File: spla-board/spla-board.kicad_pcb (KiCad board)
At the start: 4 copper layers, 178 x 107 mm, 271 parts, among them J1 USB_B_Micro, J12 J_POWER, J13 J_ANALOG, J14 J_AREF, J15 J_DPULL, J2 J_JTAG, J3 J_BODGE, J4 J_POWER2, J5 J_PPURESET, J6 J_SAMPLE, J7 Barrel_Jack, J8 J_AREF_AMP, U1 LFE5U-45F-BG256, U10 SNES_PPU1, U11 SNES_PPU2, U12 VRAM, U13 VRAM, U14 TLV73311PDBV, U15 74LVC8T245, U16 74LVC8T245, U17 74LVC8T245, U2 FT2232H, U20 74LVC8T245, U22 74LVC8T245, U23 74LVC8T245, U24 74LVC8T245, U25 74LVC8T245, U26 74LVC8T245, U27 74LVC8T245, U28 74LVC8T245, U29 74LVC8T245, U3 93LC66B, U30 74LVC8T245, U31 74LVC8T245, U32 74LVC8T245, U51 ADC1173, U52 ADC1173, U53 ADC1173, U61 LMH6611, U62 LMH6611, U63 LMH6611, U7 ST1S10PHR, U74 LMH6611, U75 LMH6611, U76 TLV73333PDBV, U8 ST1S10PHR, U9 TLV73325PDBV, X1 FT5HNBPK12.0-T1

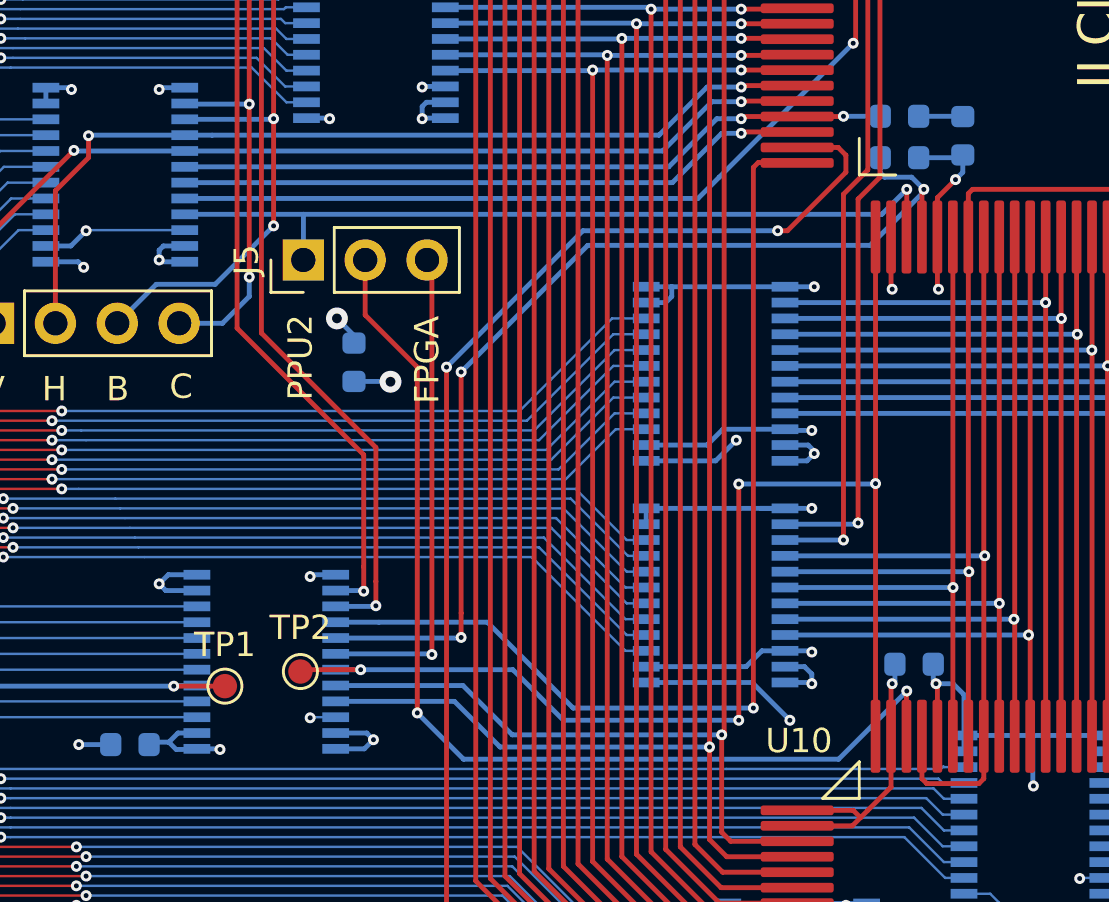
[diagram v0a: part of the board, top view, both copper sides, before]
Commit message: schematic/pcb: Move PPU RESET pulldowns before level shifter.
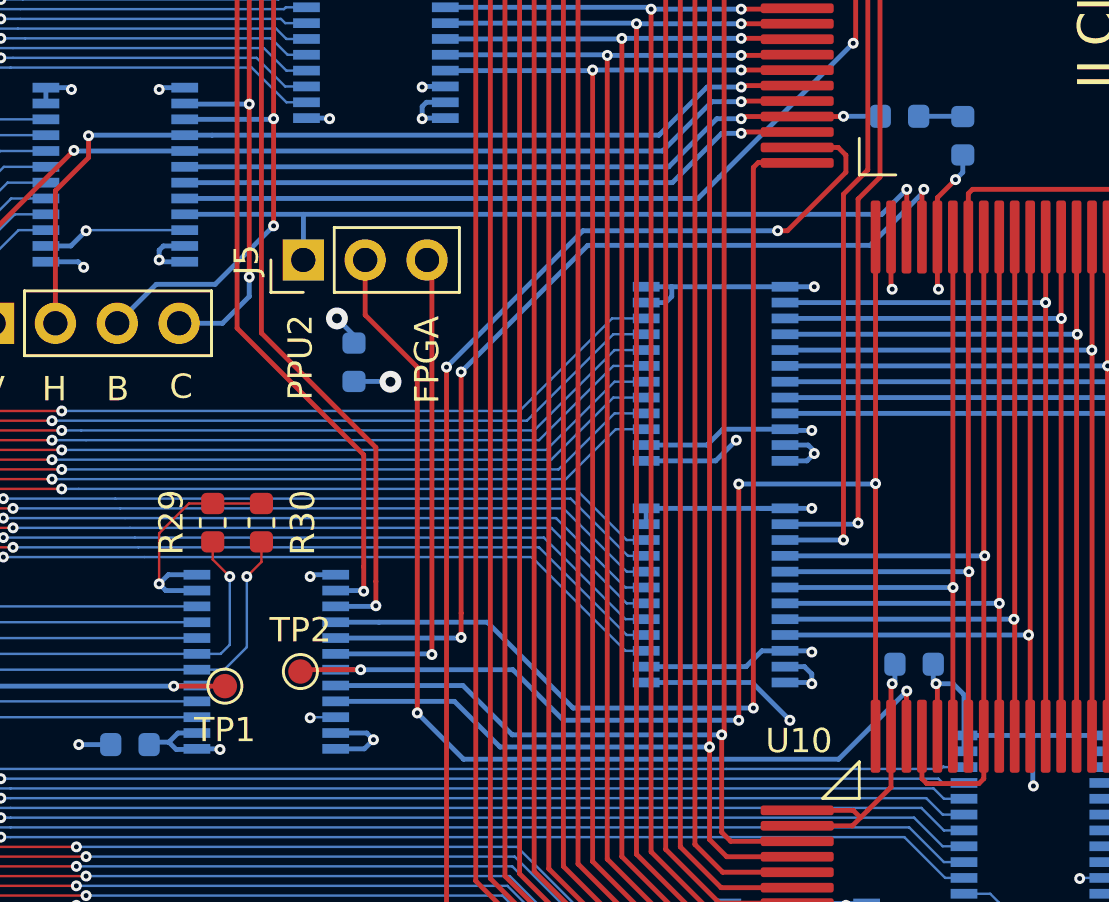
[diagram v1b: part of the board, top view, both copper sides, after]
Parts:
- added R30: 10k, Resistor_SMD:R_0603_1608Metric, F.Cu at (135.0, 100.2)
- R29: moved to F.Cu
- moved R29 31.9 mm to (133.0, 100.2), turned to 90 degrees
- renumbered R30 to R31
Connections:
- R29 pad 1: TAP_PPU2_~RESET~ -> FPGA_PPU2_~RESET~
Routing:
- net FPGA_PPU1_~RESET~: track 35.3 -> 42.3 mm, vias 1 -> 2
- net FPGA_PPU2_~RESET~: track 34.2 -> 40.2 mm, vias 1 -> 2
- net GND: track 494.1 -> 499.2 mm
- net TAP_PPU2_~RESET~: track 42.9 -> 40.2 mm

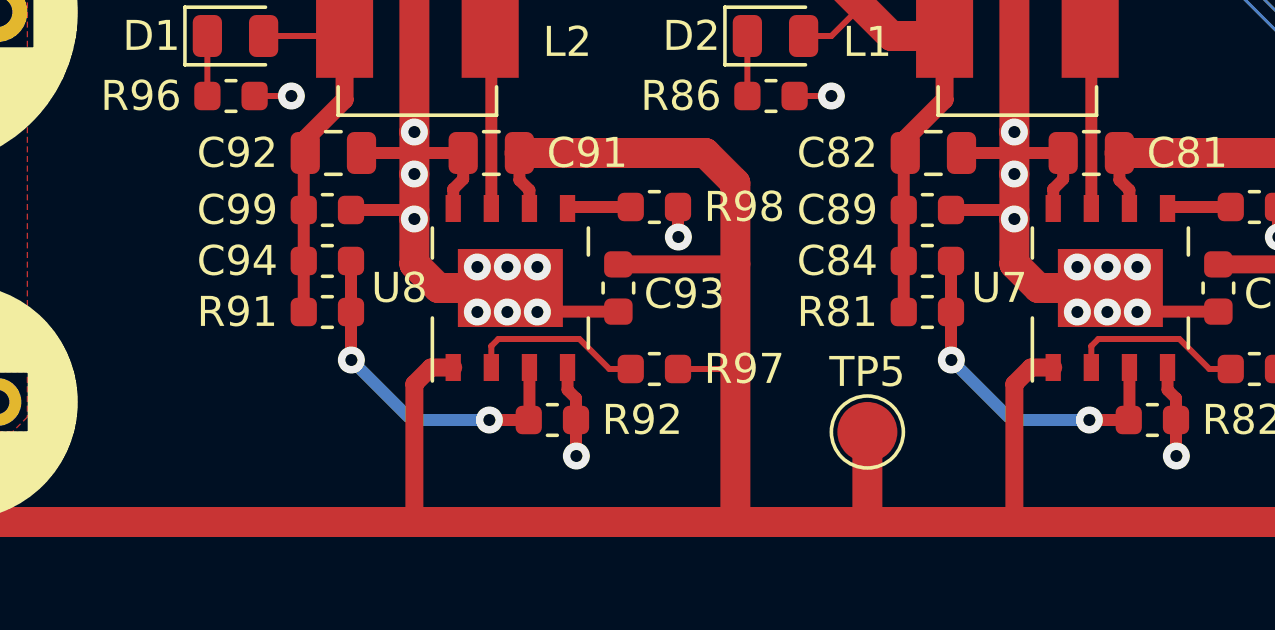
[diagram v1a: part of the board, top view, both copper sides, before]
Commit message: schematic/pcb: Complete part selection of resistors and capacitors.  Omit filters in analog block for now; adjust PCB to suit.
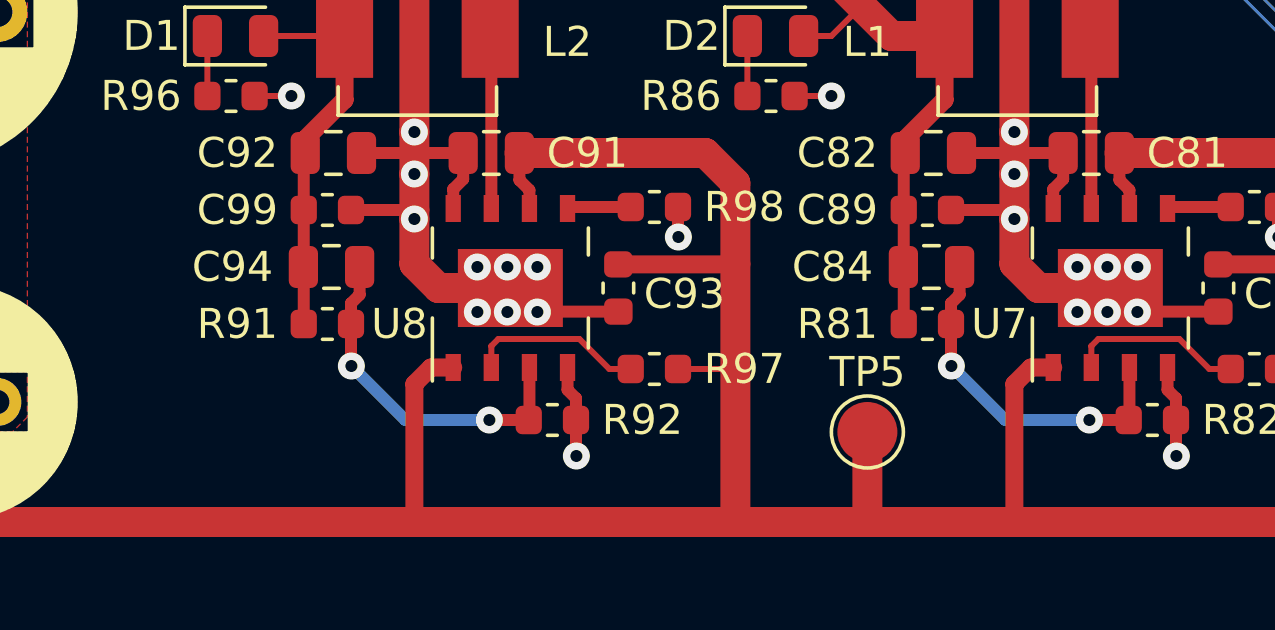
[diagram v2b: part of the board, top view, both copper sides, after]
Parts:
- C101, C102, C201, C202, C301, C302: value 1pF -> NOSTUFF
- C109, C209, C309: value 390pF -> NOSTUFF
- C7: value 3.3uF -> 4.7uF
- C84, C94: footprint Capacitor_SMD:C_0603_1608Metric -> Capacitor_SMD:C_0805_2012Metric
- R101, R102, R201, R202, R301, R302: value 16k -> 0
- R104, R204, R304: value INF -> NOSTUFF
- R109, R209, R309: value 22 -> 0
- moved R81 0.40 mm to (99.0, 144.4)
- moved R91 0.40 mm to (79.0, 144.4)
- moved C84 0.24 mm to (99.1, 142.5)
- moved C94 0.24 mm to (79.1, 142.5)

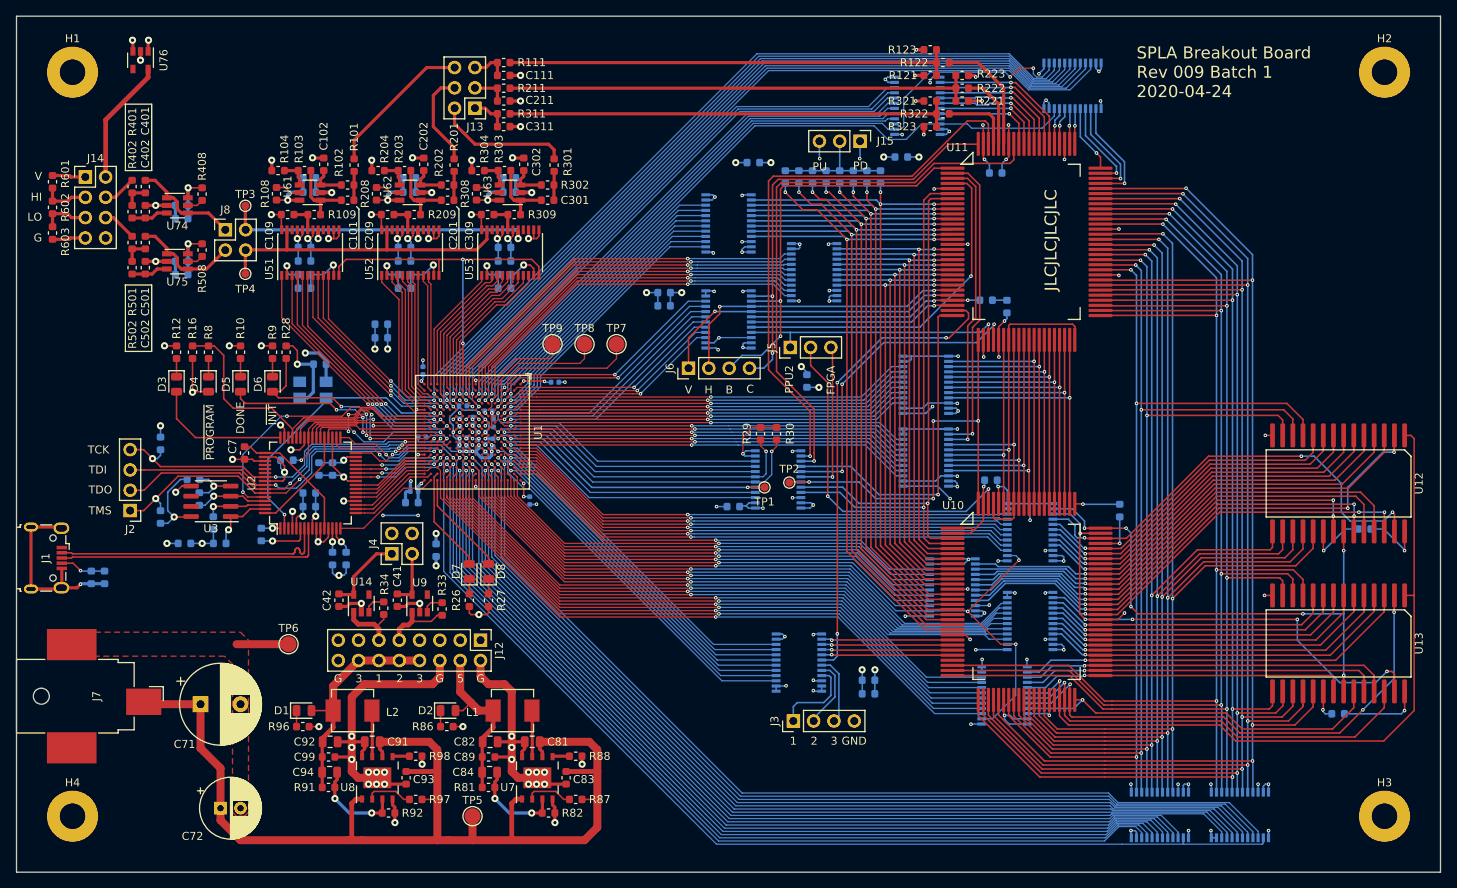
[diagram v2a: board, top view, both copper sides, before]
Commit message: pcb: Widen via-to-via distances in several places to avoid plausible drill issues.
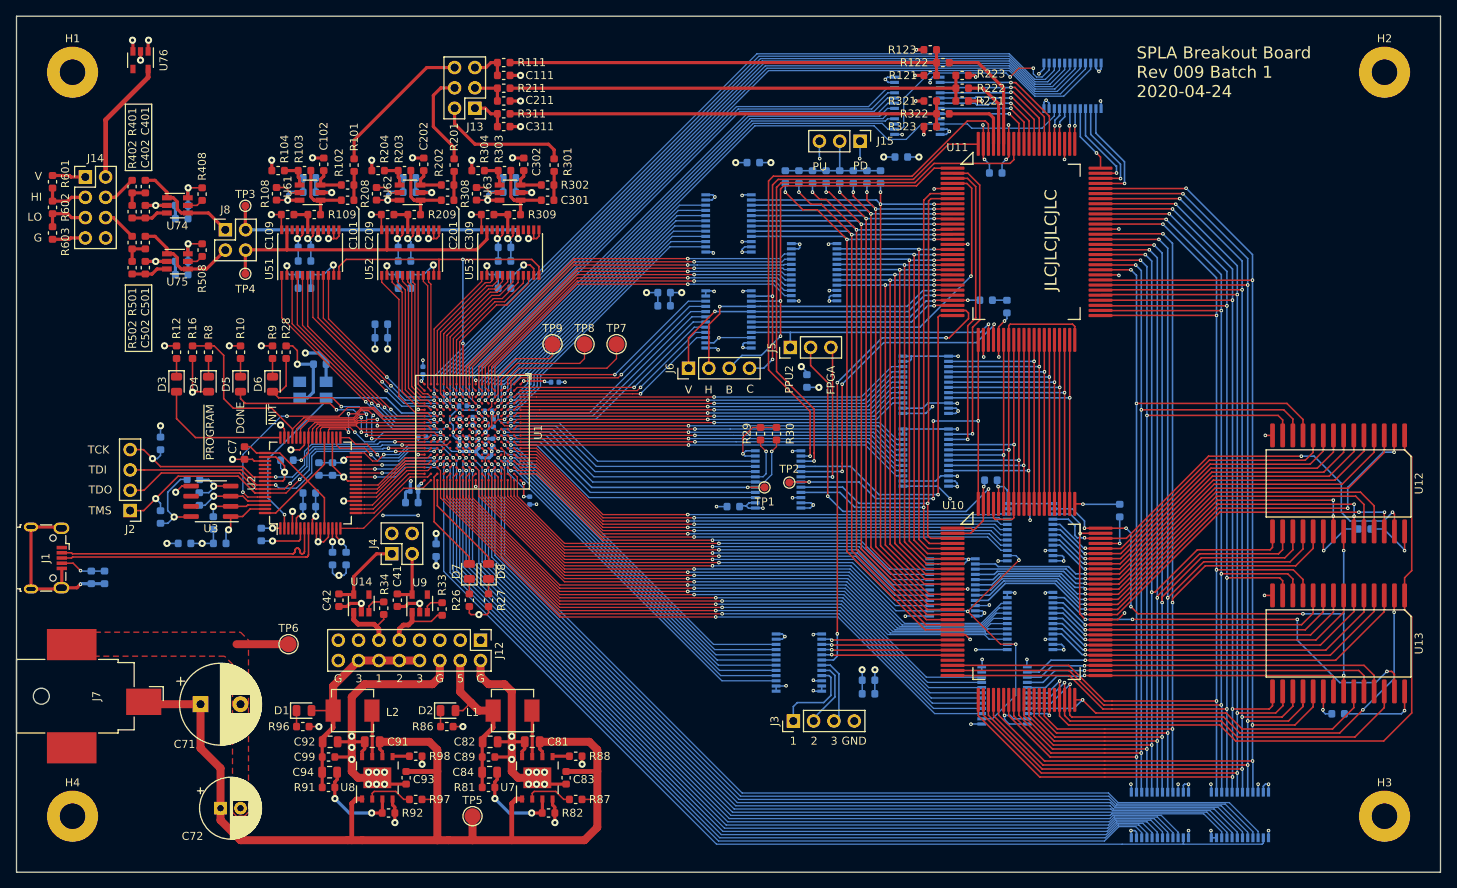
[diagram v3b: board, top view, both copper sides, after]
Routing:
- net +3V3: track 175.5 -> 174.1 mm
- net TAP_VA14: track 92.8 -> 91.7 mm
- net TAP_VDA5: track 116.2 -> 116.9 mm
- net FGPA_PPU2_TST0: track 100.9 -> 101.5 mm
- net FGPA_PPU2_TST1: track 99.8 -> 100.3 mm
- net TAP_VDA7: track 119.6 -> 120.1 mm

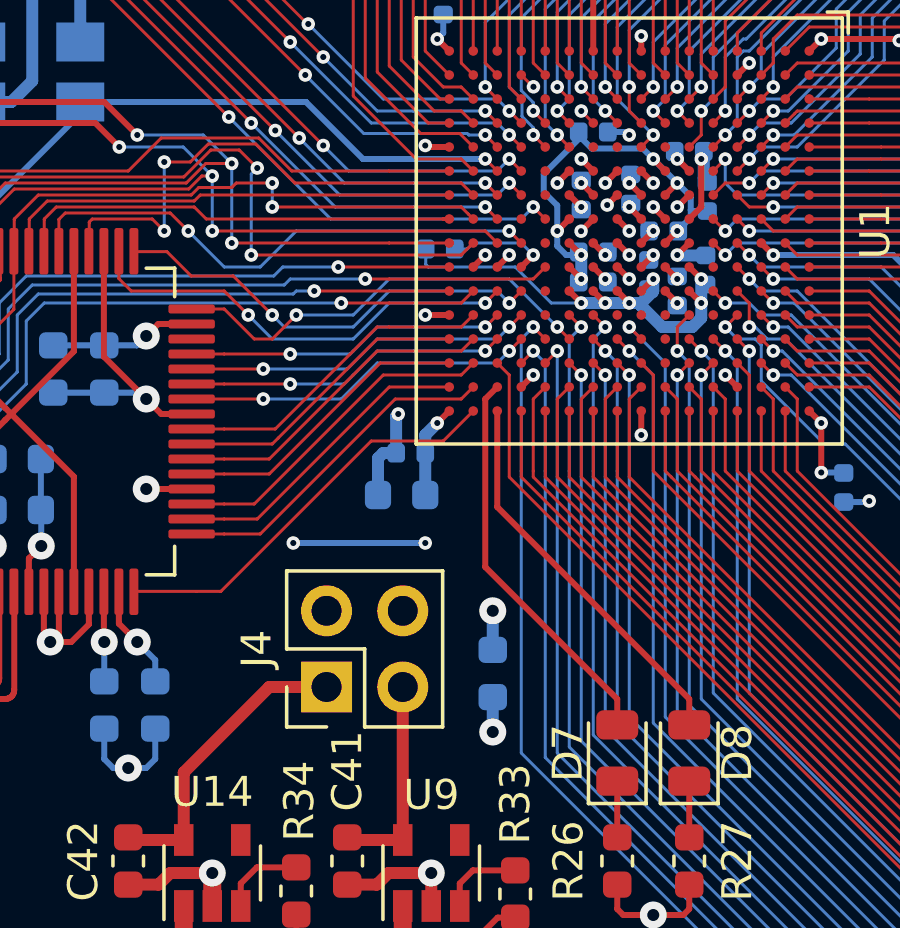
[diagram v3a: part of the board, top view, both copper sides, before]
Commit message: pcb: Shrink power/ground fill spacing to 0.2mm around FPGA.
The KiCad default here (0.508mm) is probably larger than necessary.  Also
remove most of the redundant traces that were trying to fix the fill not
getting through the gaps between vias.  I could apply this across the entire
board, but that seems like a bad idea for the larger vias.

It might be possible to reduce this further, but it's not worth the risk of an
impossible-to-fix plane-to-via short.
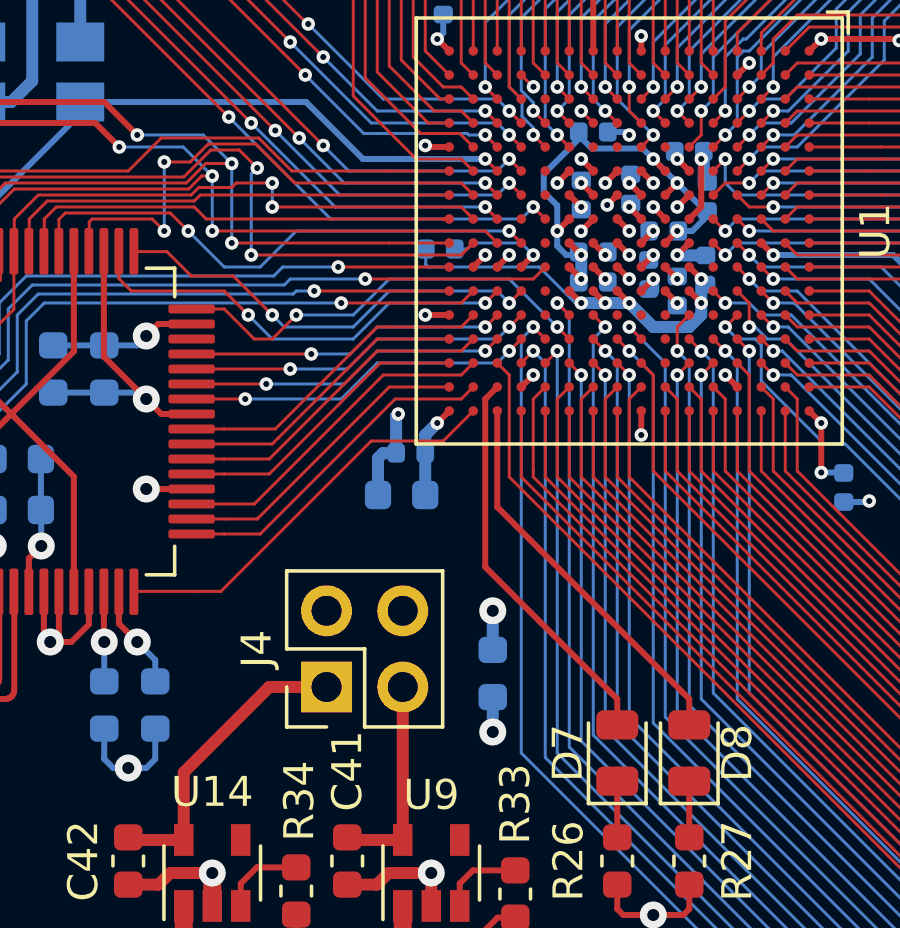
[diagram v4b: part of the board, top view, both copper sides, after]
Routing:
- net GND: track 499.0 -> 469.6 mm
- net +3V3: track 174.1 -> 153.6 mm, vias 50 -> 48
- net FPGA_VDA2: track 117.1 -> 117.9 mm

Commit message: pcb: Adjust 3.3V and 5V plane-crossing traces.
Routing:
- net +5V: track 344.2 -> 328.2 mm
- net +3V3: track 153.6 -> 157.2 mm
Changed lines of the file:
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@@
     (thickness 1.6)
     (drawings 60)
-    (tracks 4518)
+    (tracks 4513)
     (zones 0)
     (modules 272)
@@
   (layers
     (0 F.Cu signal)
-    (1 In1.Cu power)
-    (2 In2.Cu power)
+    (1 In1.Cu power hide)
+    (2 In2.Cu power hide)
     (31 B.Cu signal)
     (32 B.Adhes user)
@@
     (46 B.CrtYd user)
     (47 F.CrtYd user)
-    (48 B.Fab user)
-    (49 F.Fab user)
+    (48 B.Fab user hide)
+    (49 F.Fab user hide)
   )
   (setup
@@
   (via (at 148.4 65.6) (size 0.9) (drill 0.4) (layers F.Cu B.Cu) (net 2))
   (segment (start 149.8125 65.6) (end 148.4 65.6) (width 0.2) (layer B.Cu) (net 2))
-  (segment (start 166.3 55.2) (end 167.8 55.2) (width 0.6) (layer In2.Cu) (net 2))
-  (segment (start 160.3 64.5) (end 163.5 64.5) (width 0.6) (layer In2.Cu) (net 2))
-  (segment (start 163.5 64.5) (end 165 63) (width 0.6) (layer In2.Cu) (net 2))
-  (segment (start 154.2 65.1) (end 159.7 65.1) (width 0.6) (layer In2.Cu) (net 2))
-  (segment (start 165 56.5) (end 166.3 55.2) (width 0.6) (layer In2.Cu) (net 2))
-  (segment (start 159.7 65.1) (end 160.3 64.5) (width 0.6) (layer In2.Cu) (net 2))
-  (segment (start 165 63) (end 165 56.5) (width 0.6) (layer In2.Cu) (net 2))
   (via (at 84.8 89.6) (size 0.9) (drill 0.4) (layers F.Cu B.Cu) (net 2))
   (segment (start 84.8125 88.2) (end 84.8125 89.5875) (width 0.2) (layer B.Cu) (net 2))
@@
   (segment (start 99.4 101.6) (end 99.4 102.8) (width 0.4) (layer B.Cu) (net 2))
   (segment (start 99.4 102.8) (end 99 103.2) (width 0.4) (layer B.Cu) (net 2))
+  (segment (start 167.3 55.7) (end 167.8 55.2) (width 1) (layer In2.Cu) (net 2))
+  (segment (start 167.3 65.1) (end 167.3 55.7) (width 1) (layer In2.Cu) (net 2))
+  (segment (start 153.5 68.1) (end 164.3 68.1) (width 1) (layer In2.Cu) (net 2))
+  (segment (start 164.3 68.1) (end 167.3 65.1) (width 1) (layer In2.Cu) (net 2))
   (segment (start 71.0625 102.6) (end 70 102.6) (width 0.2) (layer F.Cu) (net 3))
   (segment (start 70 102.6) (end 69.2125 101.8125) (width 0.2) (layer F.Cu) (net 3))
@@
   (via (at 171 65.9) (size 0.45) (drill 0.2) (layers F.Cu B.Cu) (net 4))
   (segment (start 171 65.9) (end 171 63.97) (width 0.2) (layer F.Cu) (net 4))
-  (segment (start 163.7 65.9) (end 171 65.9) (width 1) (layer In2.Cu) (net 4))
-  (segment (start 160 69.6) (end 163.7 65.9) (width 1) (layer In2.Cu) (net 4))
   (segment (start 154.7 69.6) (end 160 69.6) (width 1) (layer In2.Cu) (net 4))
   (segment (start 140.36 63.621) (end 140.36 54.44) (width 1) (layer In2.Cu) (net 4))
@@
   (segment (start 150.1 109.1) (end 157 102.2) (width 1) (layer In2.Cu) (net 4))
   (segment (start 139.6 109.1) (end 150.1 109.1) (width 1) (layer In2.Cu) (net 4))
-  (segment (start 102.34 124.14) (end 122.2 144) (width 1) (layer In2.Cu) (net 4))
-  (segment (start 95.46 126) (end 95.46 124.14) (width 1) (layer In2.Cu) (net 4))
-  (segment (start 122.2 144) (end 171 144) (width 1) (layer In2.Cu) (net 4))
-  (segment (start 95.46 124.14) (end 102.34 124.14) (width 1) (layer In2.Cu) (net 4))
-  (segment (start 171 144) (end 176 139) (width 1) (layer In2.Cu) (net 4))
   (segment (start 139.675 132.375) (end 139.6 132.3) (width 0.2) (layer B.Cu) (net 4))
   (via (at 139.6 132.3) (size 0.45) (drill 0.2) (layers F.Cu B.Cu) (net 4))
@@
   (segment (start 130.7 77.15) (end 130.7 77.5) (width 0.2) (layer B.Cu) (net 4))
   (segment (start 131.025 76.825) (end 130.7 77.15) (width 0.2) (layer B.Cu) (net 4))
+  (segment (start 173 141) (end 175 139) (width 1) (layer In2.Cu) (net 4))
+  (segment (start 132 141) (end 173 141) (width 1) (layer In2.Cu) (net 4))
+  (segment (start 95.46 126) (end 95.46 124.14) (width 1) (layer In2.Cu) (net 4))
+  (segment (start 115.14 124.14) (end 132 141) (width 1) (layer In2.Cu) (net 4))
+  (segment (start 95.46 124.14) (end 115.14 124.14) (width 1) (layer In2.Cu) (net 4))
   (segment (start 163.7875 83.5) (end 163.8 83.5125) (width 0.2) (layer B.Cu) (net 5))
   (segment (start 161.9875 83.5) (end 163.7875 83.5) (width 0.2) (layer B.Cu) (net 5))
